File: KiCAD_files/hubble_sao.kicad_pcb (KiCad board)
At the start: 2 copper layers, 38 x 45.5 mm, 41 parts, among them J1 Conn_02x03_Counter_Clockwise, J2 Conn_02x03_Odd_Even, Q1 DMP3099L-7, SW1 SW_Push_Shielded, U1 VEML3328, U2 LSM6DSO, U3 ATmega328PB-A, U4 TLV9062xD, U5 TLV9062xD

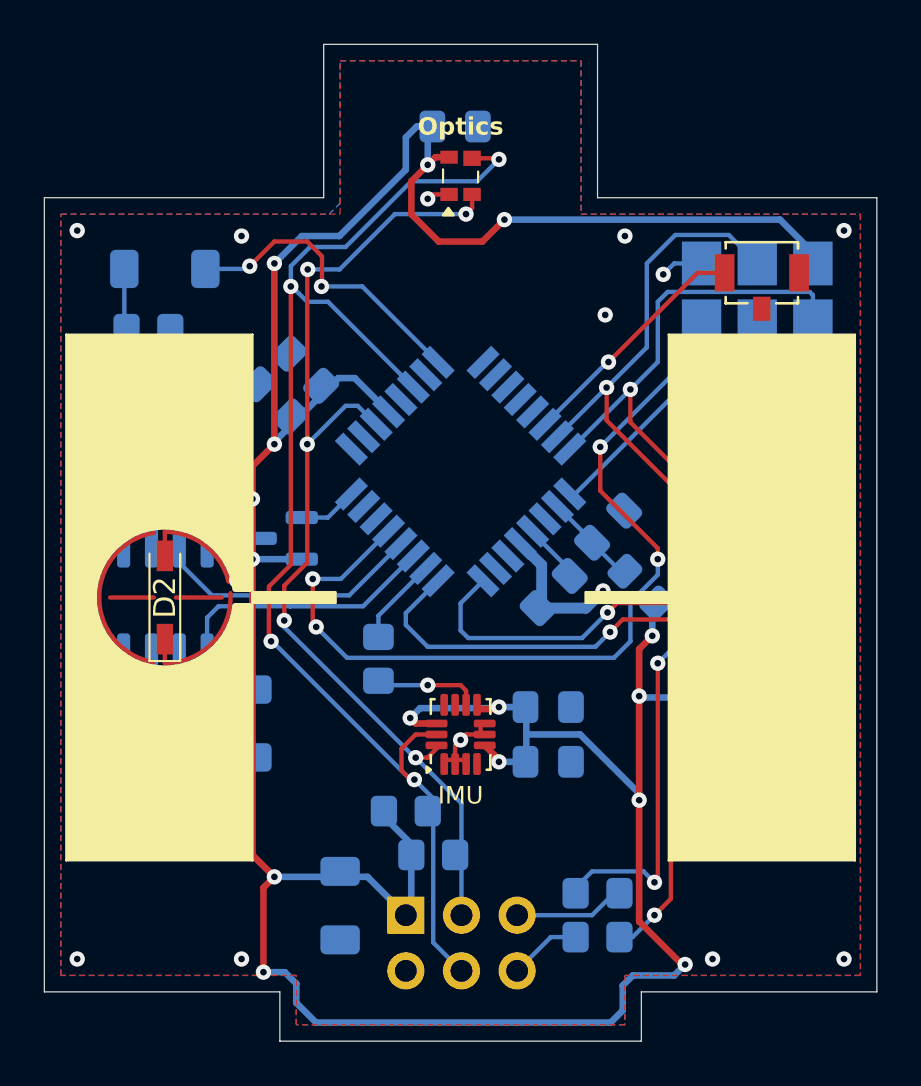
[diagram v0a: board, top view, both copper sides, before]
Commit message: Replaced back GND plane/pour by a Power (VCC) plane/pour. Rerouted traces accordingly
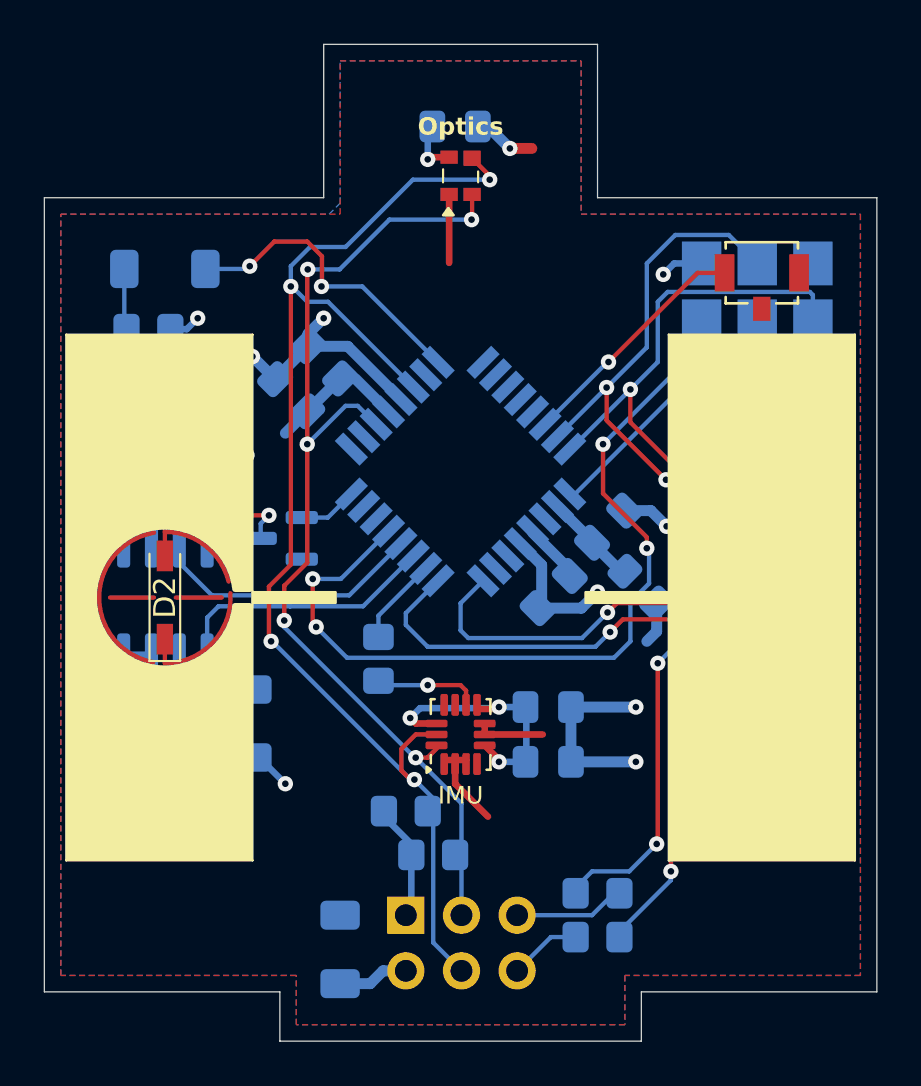
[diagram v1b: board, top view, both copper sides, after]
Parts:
- moved C12 2.00 mm to (84.5, 140.6)
- moved C2 0.93 mm to (83.8, 113.8)
- moved C11 0.80 mm to (82.3, 115.3)
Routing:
- net VCC: track 158.6 -> 31.9 mm, vias 15 -> 4
- net GND: track 13.0 -> 61.9 mm, vias 26 -> 15
- net Net-(D2-A): track 4.06 -> 7.86 mm
- net /MOSI: track 44.7 -> 43.3 mm
- net /SCL: track 60.4 -> 59.7 mm
- added copper zone on B.Cu, net VCC
- removed copper zone on B.Cu, net GND

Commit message: Cleaned up some traces
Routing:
- net Net-(D2-A): track 7.86 -> 4.33 mm
- net GND: track 61.9 -> 60.5 mm
- net /LED: track 14.3 -> 12.9 mm
- net /PANEL3: track 23.3 -> 22.1 mm
- net /PANEL4: track 26.0 -> 25.2 mm
- net VCC: track 31.9 -> 32.6 mm

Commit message: Changed RX/TX resistors to 470Ohm for short circuit protection
Fixes #4
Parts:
- R11, R2: value 0 -> 470
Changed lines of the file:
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@@
 			)
 		)
-		(property "Value" "0"
+		(property "Value" "470"
 			(at 0 -1.65 0)
 			(layer "B.Fab")
@@
 			)
 		)
-		(property "Value" "0"
+		(property "Value" "470"
 			(at 0 -1.65 0)
 			(layer "B.Fab")

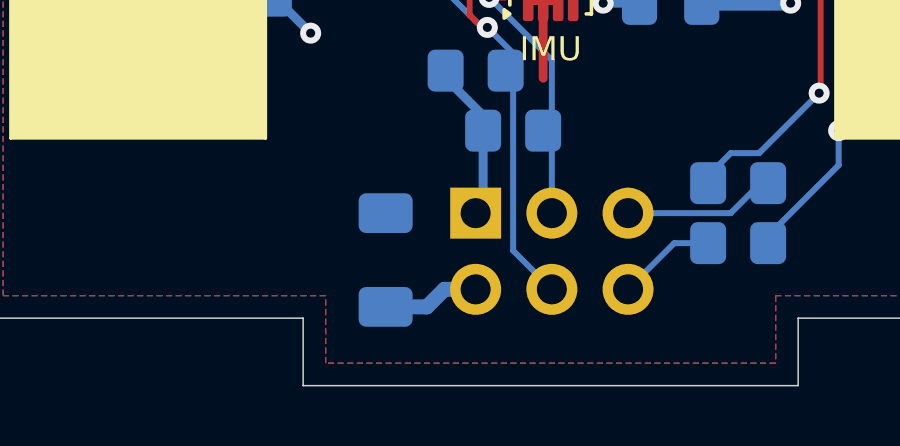
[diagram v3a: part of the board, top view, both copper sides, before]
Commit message: Created keep out around pin header
- To enhance hand soldering (hopefully)
- To still have soldermask instead of bare FR4 (was not the case before)
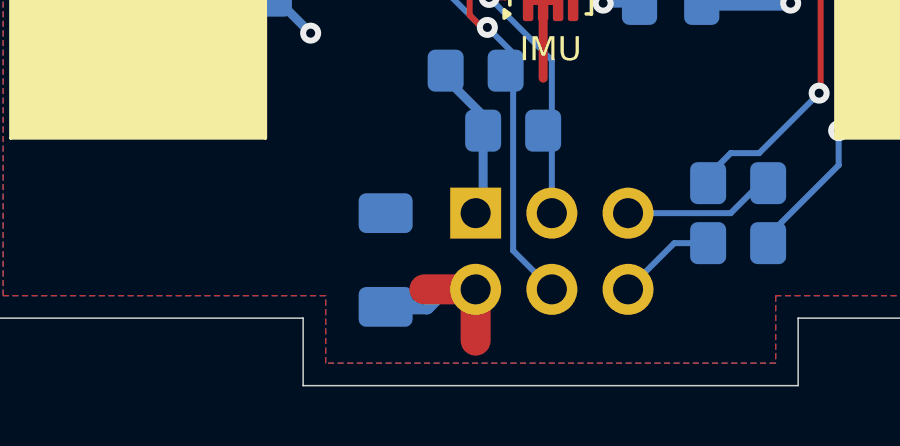
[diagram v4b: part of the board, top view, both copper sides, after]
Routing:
- net GND: track 60.5 -> 63.9 mm
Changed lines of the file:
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@@
+	)
+	(segment
+		(start 87.5 141.54)
+		(end 87.5 143.25)
+		(width 1)
+		(layer "F.Cu")
+		(net 20)
+	)
+	(segment
+		(start 87.5 141.54)
+		(end 85.79 141.54)
+		(width 1)
+		(layer "F.Cu")
+		(net 20)
 	)
 	(segment
@@
 			)
 		)
+	)
+	(zone
+		(net 0)
+		(net_name "")
+		(layers "F.Cu" "F.Mask")
+		(name "Keep_out_pin_header")
+		(hatch edge 0.5)
+		(connect_pads
+			(clearance 0)
+		)
+		(min_thickness 0.25)
+		(filled_areas_thickness no)
+		(keepout
+			(tracks allowed)
+			(vias allowed)
+			(pads allowed)
+			(copperpour not_allowed)
+			(footprints allowed)
+		)
+		(fill
+			(thermal_gap 0.5)
+			(thermal_bridge_width 0.5)
+		)
+		(polygon
+			(pts
+				(xy 86.05 138.15) (xy 86.65 137.55) (xy 93.45 137.55) (xy 94.05 138.15) (xy 94.05 142.4) (xy 93.45 143)
+				(xy 86.65 143) (xy 86.05 142.4)
+			)
+		)

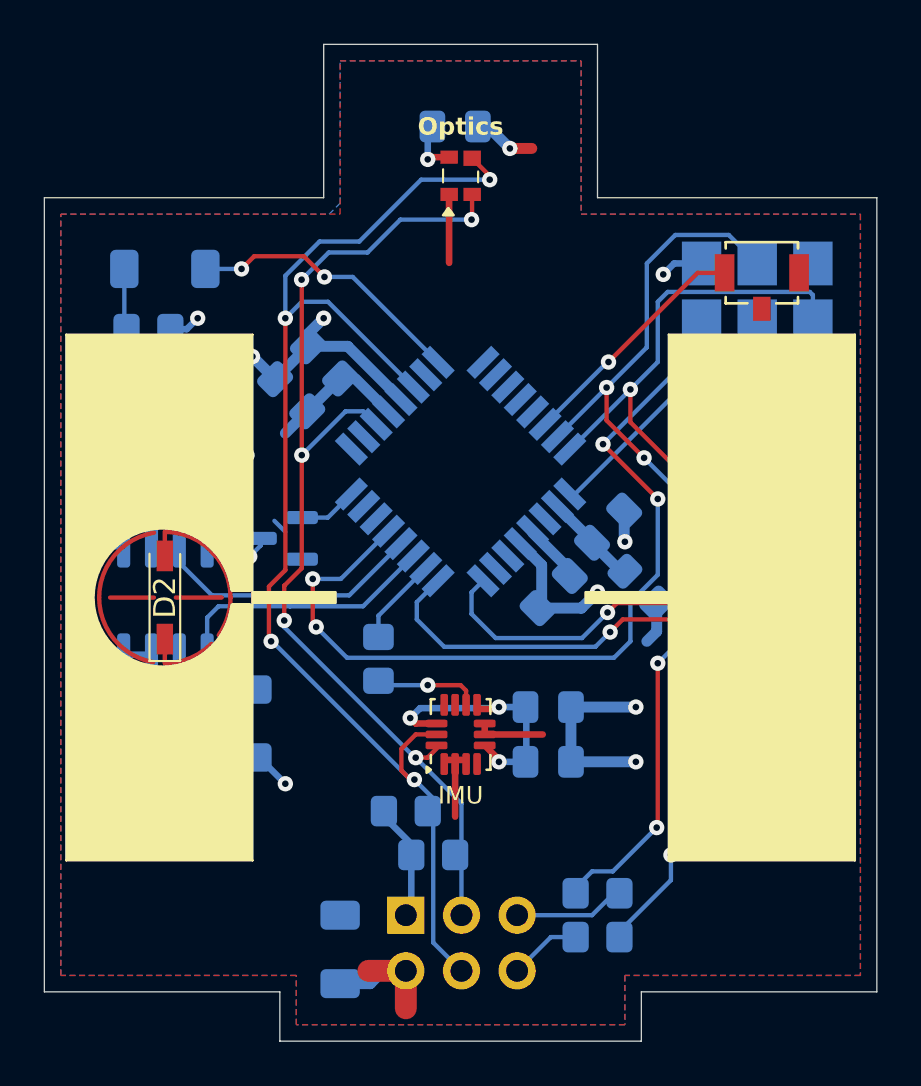
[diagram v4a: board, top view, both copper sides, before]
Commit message: Moved ICSP pads for an easier pogo pins positionning
The ICSP pads are now positionned to be approx 0.1" and 0.2" from
the board's sides. This means that alignement pins on a 0.1" grid
can be used on the pogrammer's side to accurately position the
pogo pins while programming. See User1 Layer for more info.
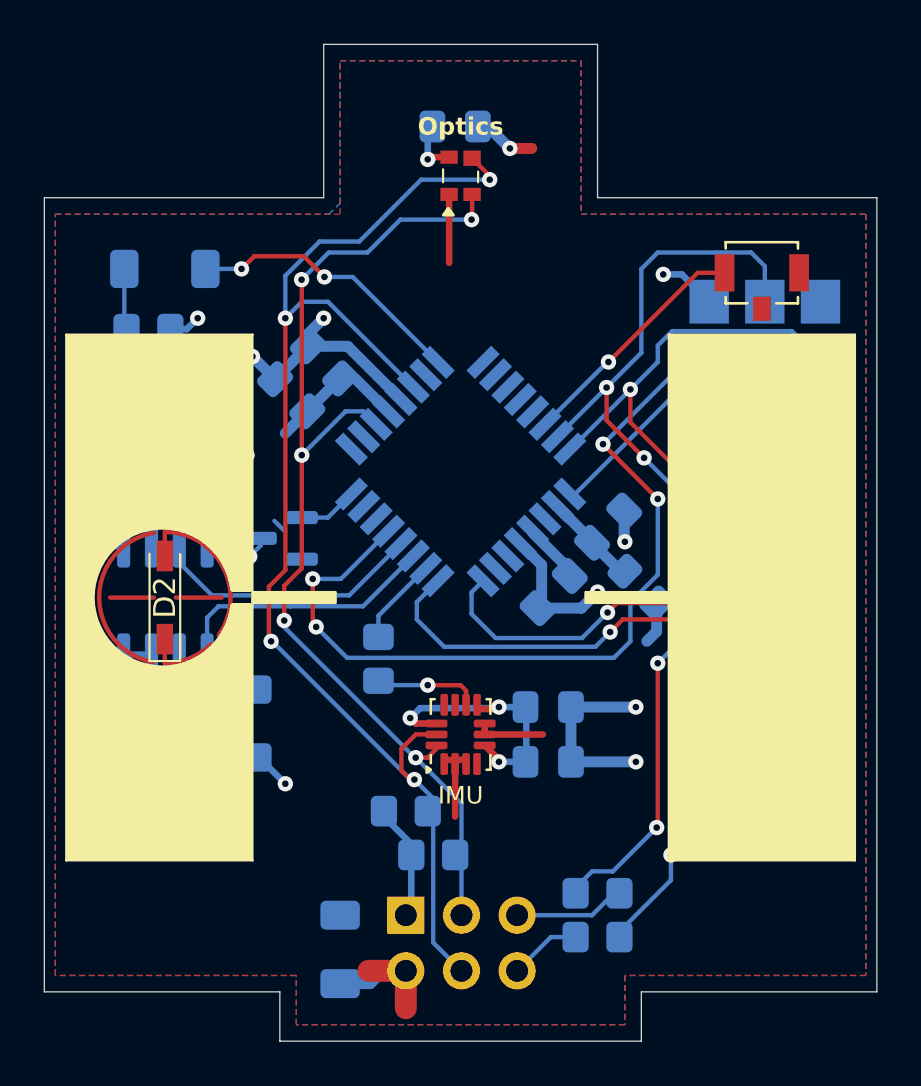
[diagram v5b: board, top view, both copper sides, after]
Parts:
- moved J1 1.78 mm to (103.9, 112.3)
- moved C8 0.25 mm to (103.8, 119.2)
- moved R3 0.25 mm to (103.8, 117.2)
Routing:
- net /MISO: track 44.7 -> 42.4 mm
- net VCC: track 32.6 -> 34.0 mm
- net /MOSI: track 42.9 -> 44.2 mm
- net /RST: track 39.9 -> 38.9 mm
- net GND: track 63.9 -> 64.5 mm
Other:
- board text added: "Alignement pins"
- board text added: "Pogo pins"

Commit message: Changed the manufacturer string/id to a default one
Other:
- board text added: "MfgStr"
- board text removed: "WayWayWay"
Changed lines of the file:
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@@
 		)
 	)
-	(gr_text "WayWayWay"
-		(at 79.75 140.25 0)
+	(gr_text "MfgStr"
+		(at 76.2 139.7 0)
 		(layer "B.SilkS")
 		(effects
@@
 				(bold yes)
 			)
-			(justify left bottom mirror)
+			(justify mirror)
 		)
 	)

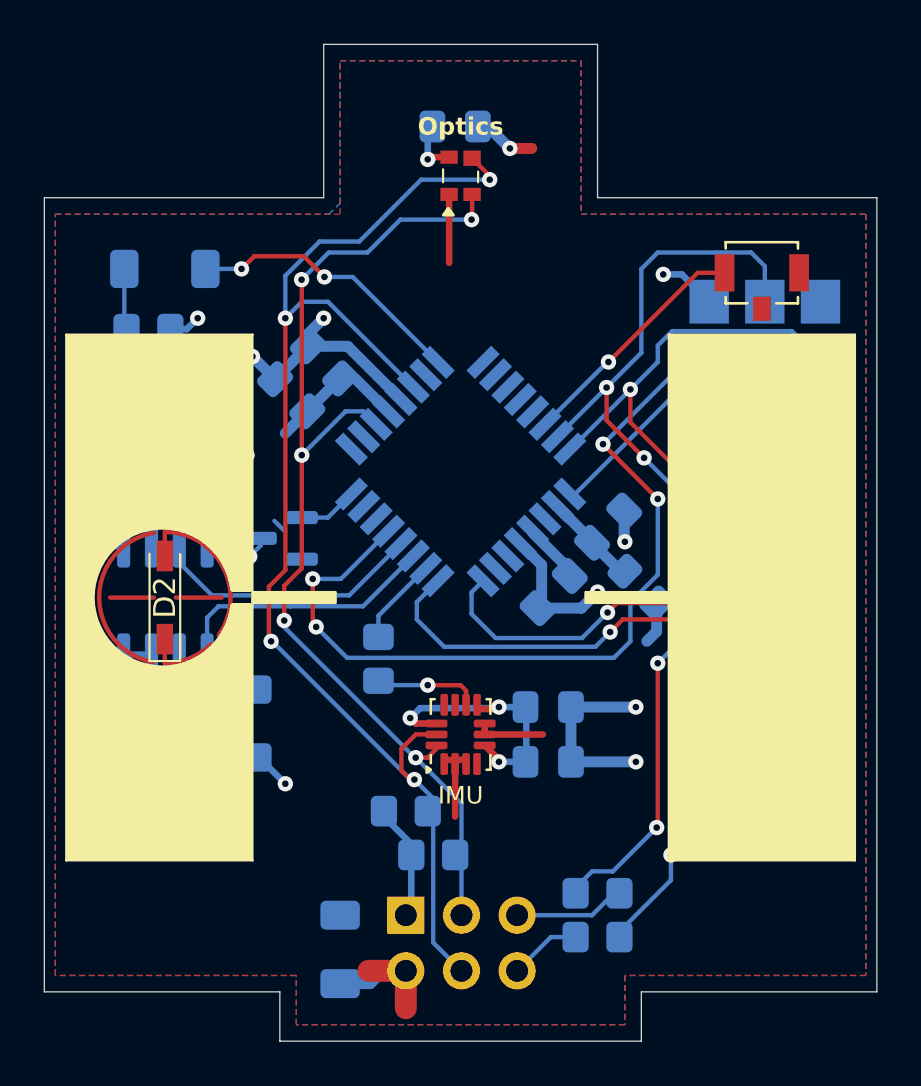
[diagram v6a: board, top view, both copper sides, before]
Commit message: Modified RESET circuitry
- Added a switch to multiplex RESET and SCL on the pin header
- Added short-circuit protection on the RESET pin
- Added missing pullup resistor on the RESET pin. Before, RESET
was left floating. No problem was noticed on the prototype.
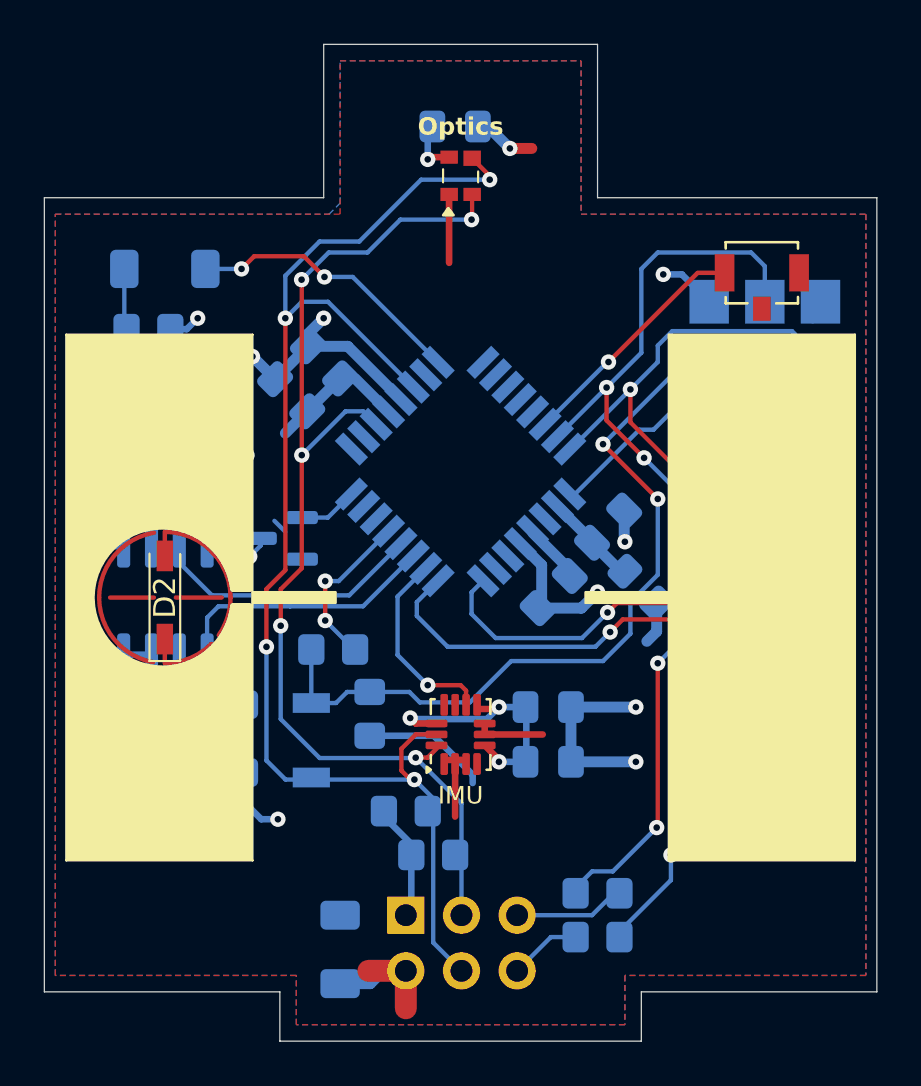
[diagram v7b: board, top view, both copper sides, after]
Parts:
- added R12: 220, Resistor_SMD:R_0805_2012Metric_Pad1.20x1.40mm_HandSolder, B.Cu at (84.2, 126.9)
- added SW2: SW_Push, Button_Switch_SMD:SW_SPST_B3U-1000P, B.Cu at (83.2, 131.0)
- R8: value 0 -> 10k
- moved R8 2.54 mm to (85.9, 129.8), turned to -90 degrees
- moved R9 0.92 mm to (79.9, 130.9)
- moved R10 0.43 mm to (76.8, 132.2)
- moved C10 0.39 mm to (76.9, 130.2)
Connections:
- J1 pad 3: /RST -> /RST_ICSP
- R8 pad 1: Net-(U2-INT2) -> /RST_ICSP
- R8 pad 2: /INT1_IMU -> VCC
- U2 pad 9: Net-(U2-INT2) -> /INT1_IMU
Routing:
- net /RST_ICSP: track 0.00 -> 35.4 mm, vias 0 -> 2
- net /RST: track 38.9 -> 7.56 mm, vias 4 -> 2
- net VCC: track 34.0 -> 39.9 mm
- net /INT1_IMU: track 3.47 -> 8.94 mm, vias 0 -> 1
- net Net-(U2-INT2): track 4.84 -> 0.00 mm, vias 1 -> 0
- net /SCL: track 59.9 -> 63.3 mm
- net /SDA: track 48.6 -> 51.3 mm
- net GND: track 64.5 -> 65.9 mm
